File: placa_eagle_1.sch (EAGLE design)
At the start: 25 parts, among them J2 CONN_0227-2021, J3 CONN_0227-2021, J4 CONN_0227-2021, J5 CONN_0327-2031, J6 CONN_0327-2031

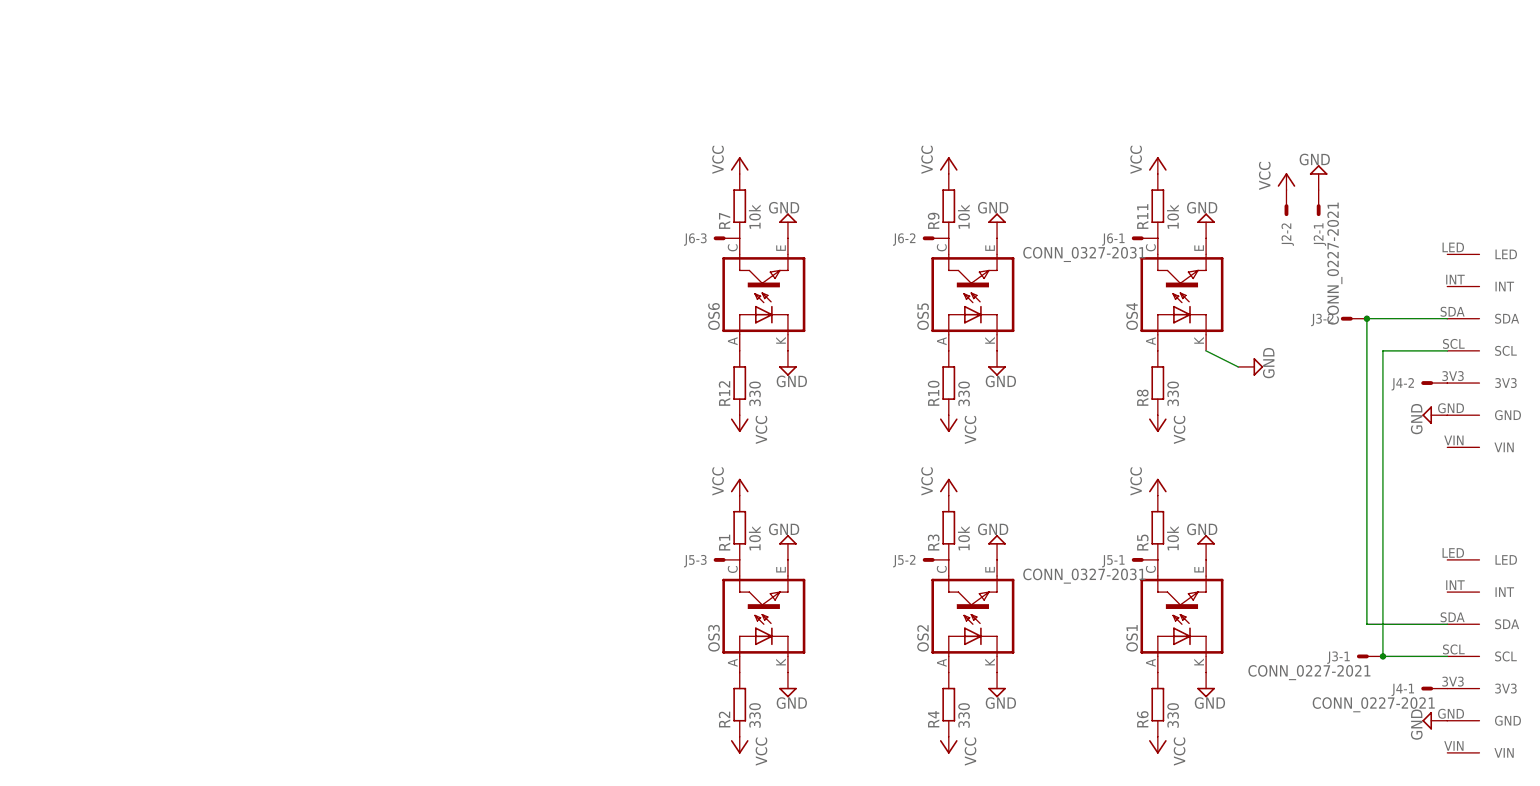
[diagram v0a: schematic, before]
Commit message: Placa:
foi alterado a distância dos sensores.
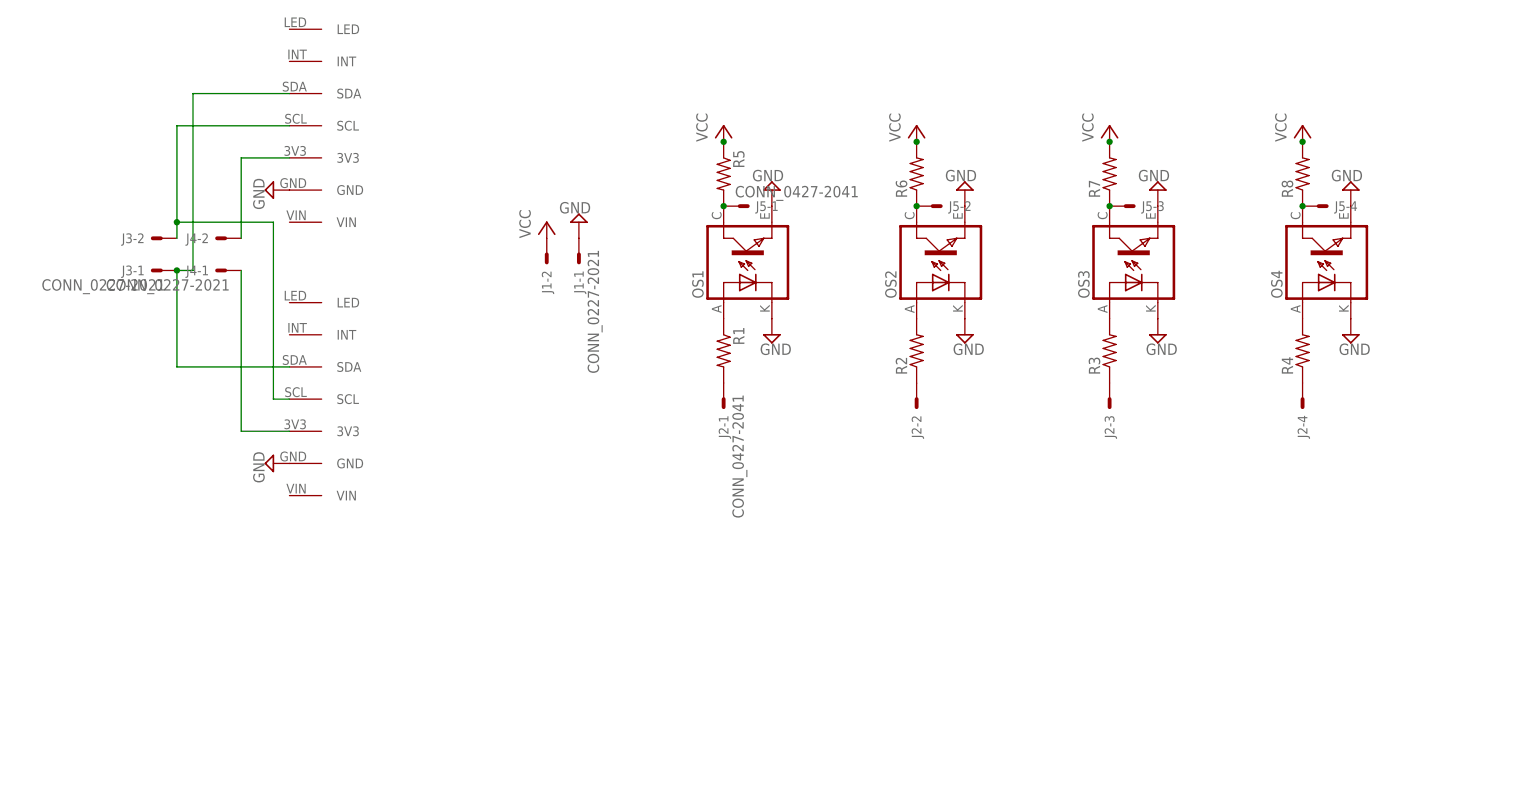
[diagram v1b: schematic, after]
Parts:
- removed J6: CONN_0327-2031, Robotica-IFRN-SC-conectores:CONN_0327-2031
- removed OS5, OS6: (no value), Robotica-IFRN-SC-sensores:TCRT5000
- removed R10, R12: 330, rcl:R-EU_0204/7
- removed R11, R9: 10k, rcl:R-EU_0204/7
- added J1: CONN_0227-2021, Robotica-IFRN-SC-conectores:CONN_0227-2021
- J2: value CONN_0227-2021 -> CONN_0427-2041; device Robotica-IFRN-SC-conectores:CONN_0227-2021 -> Robotica-IFRN-SC-conectores:CONN_0427-2041
- J5: value CONN_0327-2031 -> CONN_0427-2041; device Robotica-IFRN-SC-conectores:CONN_0327-2031 -> Robotica-IFRN-SC-conectores:CONN_0427-2041
- R1, R3, R5, R7: value 10k -> (none); device rcl:R-EU_0204/7 -> rcl:R-US_0204/7
- R2, R4, R6, R8: value 330 -> (none); device rcl:R-EU_0204/7 -> rcl:R-US_0204/7
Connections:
- removed net N$13 (its old number): J3-1.S, TCS1.SCL, TCS2.SCL
- new net N$18: J3-2.S, TCS1.SCL, TCS2.SCL
- net GND: now also J1-1.S; no longer J2-1.S, OS5.CATHODE, OS5.EMITTER, OS6.CATHODE, OS6.EMITTER
- net N$1: now also OS1.ANODE, R1.1; no longer J5-1.S, OS1.COLLECTOR, R5.1
- net N$10: now also J2-2.S, R2.1; no longer OS2.ANODE, R4.2
- net N$11: now also J2-3.S, R3.1; no longer OS3.ANODE, R2.2
- net N$12: now also J2-4.S, R4.1; no longer J3-2.S, TCS1.SDA, TCS2.SDA
- net N$16: now also J3-1.S, TCS1.SDA, TCS2.SDA; no longer OS4.ANODE, R8.2
- net N$2: now also OS2.ANODE, R2.2; no longer OS5.ANODE, R10.2
- net N$3: now also OS3.ANODE, R3.2; no longer J6-1.S, OS4.COLLECTOR, R11.1
- net N$4: now also OS4.ANODE, R4.2; no longer J6-2.S, OS5.COLLECTOR, R9.1
- net N$5: now also J5-1.S, OS1.COLLECTOR, R5.2; no longer J6-3.S, OS6.COLLECTOR, R7.1
- net N$6: now also J5-2.S, OS2.COLLECTOR, R6.1; no longer OS6.ANODE, R12.2
- net N$7: now also J5-3.S, OS3.COLLECTOR, R7.1; no longer J5-2.S, OS2.COLLECTOR, R3.1
- net N$8: now also J5-4.S, OS4.COLLECTOR, R8.1; no longer J5-3.S, OS3.COLLECTOR, R1.1
- net N$9: now also J2-1.S, R1.2; no longer OS1.ANODE, R6.2
- net VCC: now also J1-2.S, R5.1, R6.2, R8.2; no longer J2-2.S, R1.2, R10.1, R11.2, R12.1, R2.1, R3.2, R4.1, R5.2, R6.1, R8.1, R9.2
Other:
- moved on the sheet: J2-1, J2-2, J3-1, J3-2, J4-1, J4-2, J5-1, J5-2, J5-3, OS1, OS2, OS3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
